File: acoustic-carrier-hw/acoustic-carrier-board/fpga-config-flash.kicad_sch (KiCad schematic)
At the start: 21 parts, among them IC1 ECP5-BGA256, J701 Conn_02x03_Odd_Even, J702 PMOD_JTAG, J703 PMOD_SPI, U701 W25Q128JVS, U702 W25Q128JVS

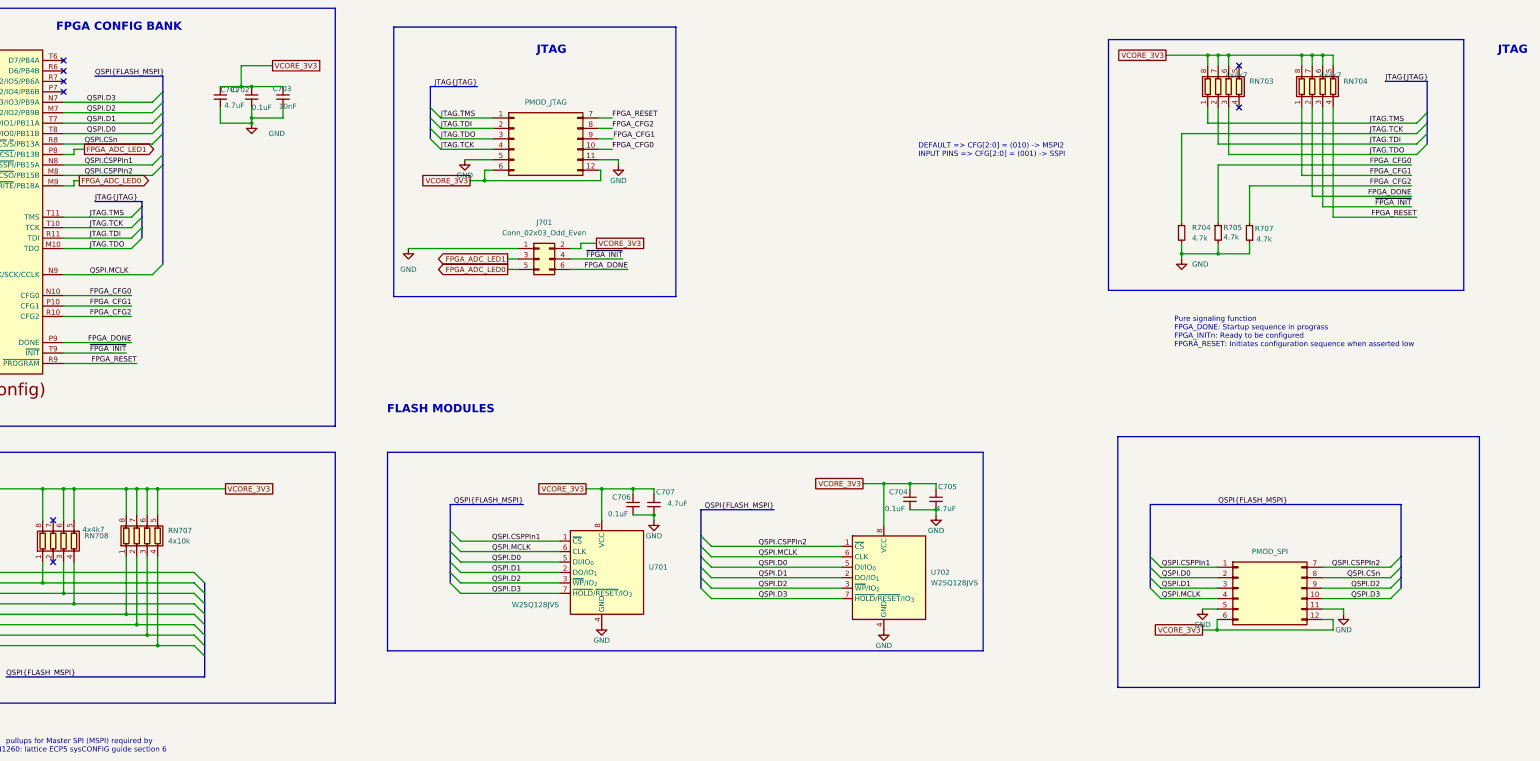
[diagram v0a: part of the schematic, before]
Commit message: [carrier] Added 2 buttons and 2 leds + routing
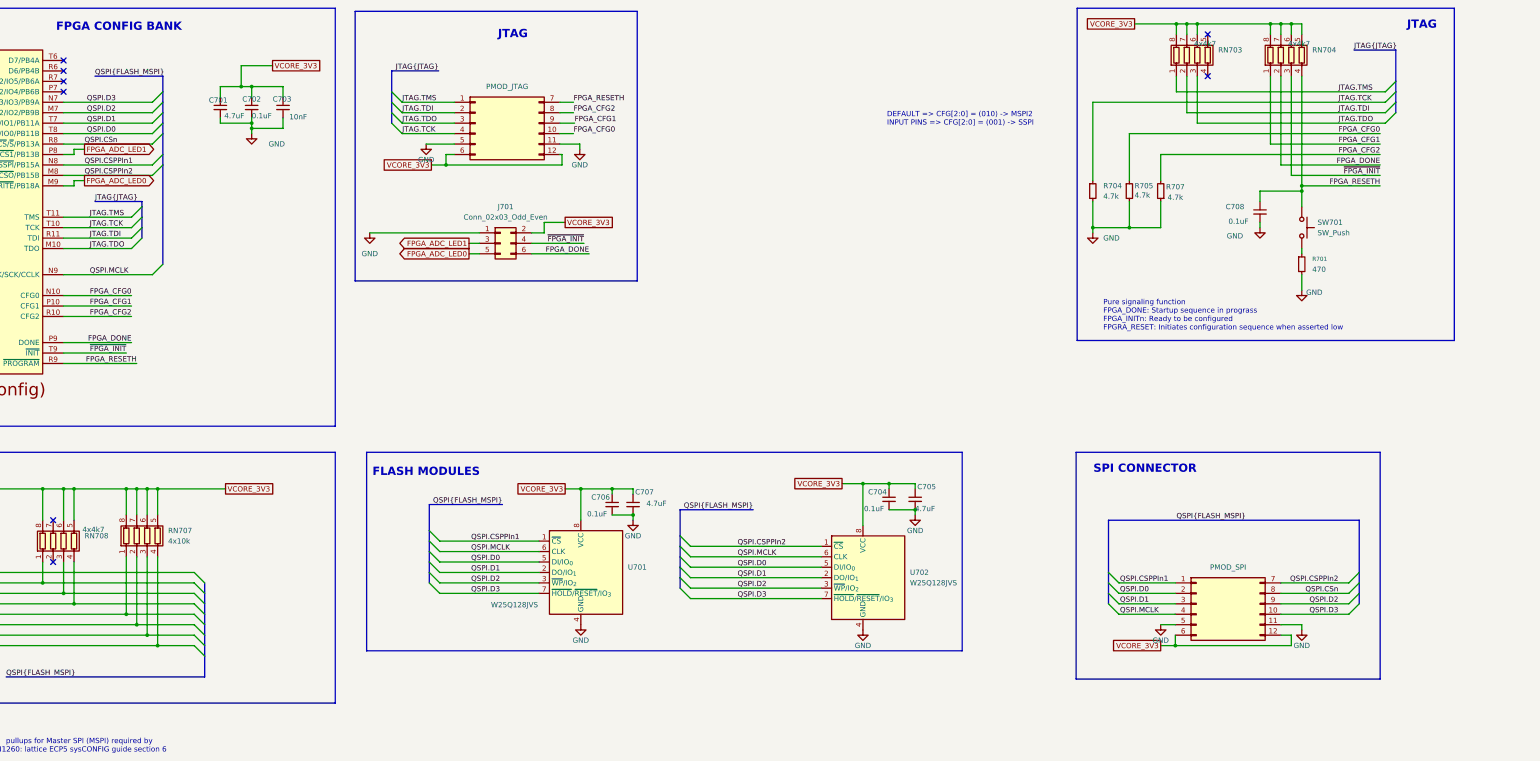
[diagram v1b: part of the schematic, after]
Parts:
- added C708: 0.1uF, Capacitor_SMD:C_0201_0603Metric, symbol Device:C_Small
- added R701: 470, Resistor_SMD:R_0402_1005Metric, symbol Device:R_Small
- added SW701: SW_Push, iw-misc:SW_TS-1088-AR02016, symbol Switch:SW_Push
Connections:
- net GND: now also C708.2, R701.2
- net FPGA_RESET renamed FPGA_RESETH
- net FPGA_RESETH: now also C708.1, SW701.1
- new net: R701.1, SW701.2
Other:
- note added: "SPI CONNECTOR"
- moved on the sheet: C701, C702, C703, C704, C705, C706, C707, J701, R704, R705, R707, RN703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

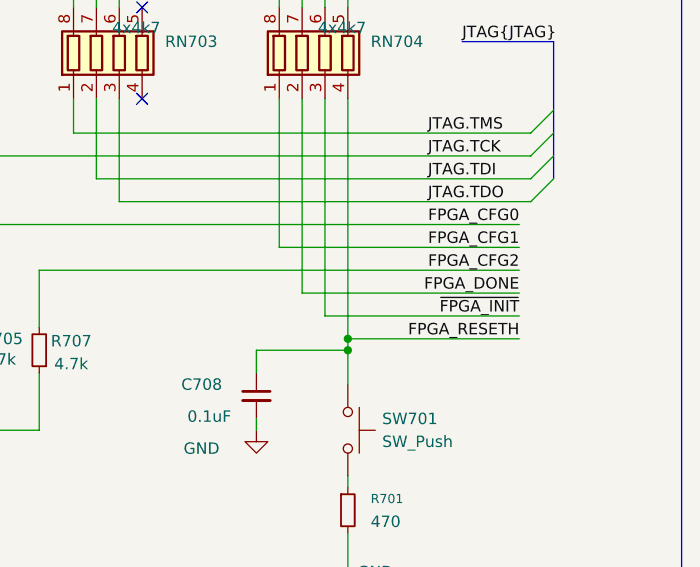
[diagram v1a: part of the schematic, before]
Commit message: [carrier] Added decoupling to LPDDR3 and routed VREF (next) finalize power supply
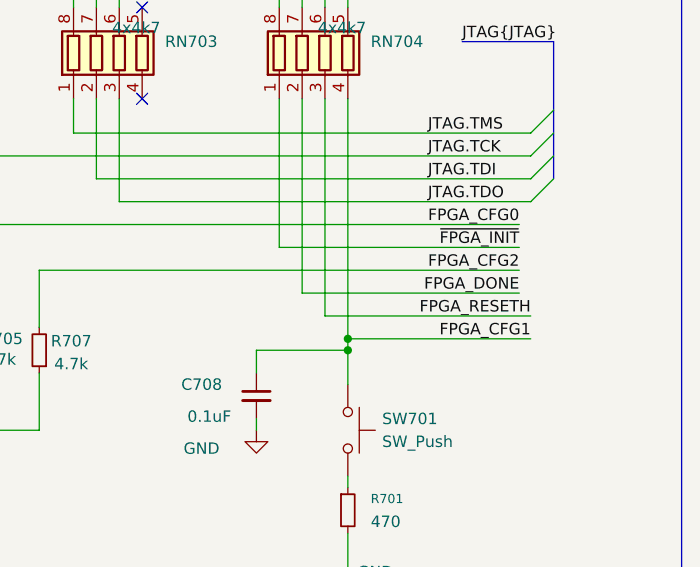
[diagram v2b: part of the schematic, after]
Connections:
- net FPGA_CFG1: now also C708.1, RN704.4 (R4.1), SW701.1; no longer RN704.1 (R1.1)
- net FPGA_RESETH: now also RN704.3 (R3.1); no longer C708.1, RN704.4 (R4.1), SW701.1
- net ~{FPGA_INIT}: now also RN704.1 (R1.1); no longer RN704.3 (R3.1)
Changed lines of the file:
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@@
 	(wire
 		(pts
-			(xy 381 59.69) (xy 361.95 59.69)
+			(xy 361.95 59.69) (xy 382.27 59.69)
 		)
 		(stroke
@@
 	(wire
 		(pts
-			(xy 381 54.61) (xy 356.87 54.61)
+			(xy 356.87 54.61) (xy 381 54.61)
 		)
 		(stroke
@@
 	(wire
 		(pts
-			(xy 381 57.15) (xy 359.41 57.15)
+			(xy 359.41 57.15) (xy 382.27 57.15)
 		)
 		(stroke
@@
 	(wire
 		(pts
-			(xy 381 49.53) (xy 354.33 49.53)
+			(xy 354.33 49.53) (xy 381 49.53)
 		)
 		(stroke
@@
 			(width 0)
 			(type default)
+		)
+	)
+	(label "FPGA_DONE"
+		(at 381 54.61 180)
+		(effects
+			(font
+				(size 1.27 1.27)
+			)
+			(justify right bottom)
 		)
 	)
@@
 		)
 	)
-	(label "FPGA_CFG1"
-		(at 381 49.53 180)
-		(effects
-			(font
-				(size 1.27 1.27)
-			)
-			(justify right bottom)
-		)
-	)
 	(label "JTAG.TMS"
 		(at 143.256 39.37 0)
@@
 		)
 	)
-	(label "FPGA_DONE"
-		(at 381 54.61 180)
-		(effects
-			(font
-				(size 1.27 1.27)
-			)
-			(justify right bottom)
-		)
-	)
 	(label "FPGA_RESETH"
-		(at 381 59.69 180)
+		(at 382.27 57.15 180)
 		(effects
 			(font
@@
 		)
 	)
+	(label "FPGA_CFG1"
+		(at 382.27 59.69 180)
+		(effects
+			(font
+				(size 1.27 1.27)
+			)
+			(justify right bottom)
+		)
+	)
 	(label "QSPI.D0"
 		(at 27.94 163.83 0)
@@
 	)
 	(label "~{FPGA_INIT}"
-		(at 381 57.15 180)
-		(effects
-			(font
-				(size 1.27 1.27)
-			)
-			(justify right bottom)
-		)
-	)
-	(label "~{FPGA_INIT}"
 		(at 76.2 100.33 180)
 		(effects
@@
 		)
 	)
+	(label "~{FPGA_INIT}"
+		(at 381 49.53 180)
+		(effects
+			(font
+				(size 1.27 1.27)
+			)
+			(justify right bottom)
+		)
+	)

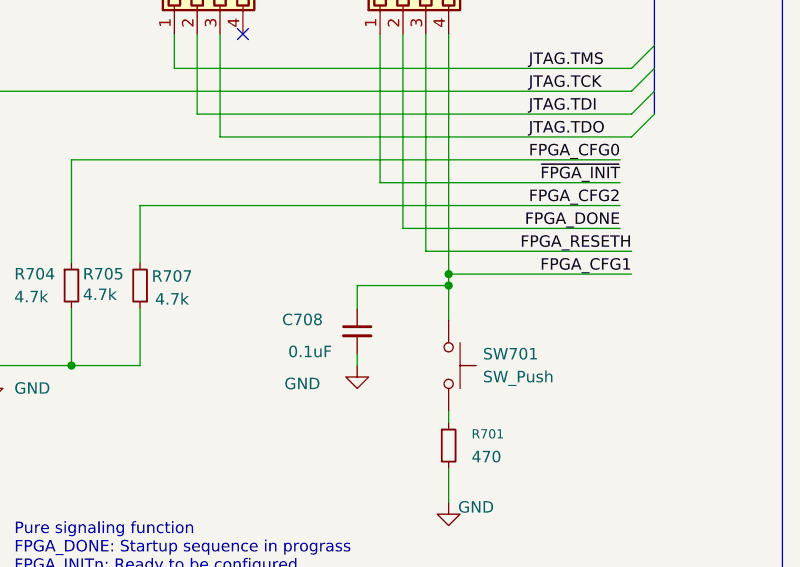
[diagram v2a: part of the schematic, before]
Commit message: [carrier] Corrected most of the DRC errors, a  few tens left + respacing DDR3-traces
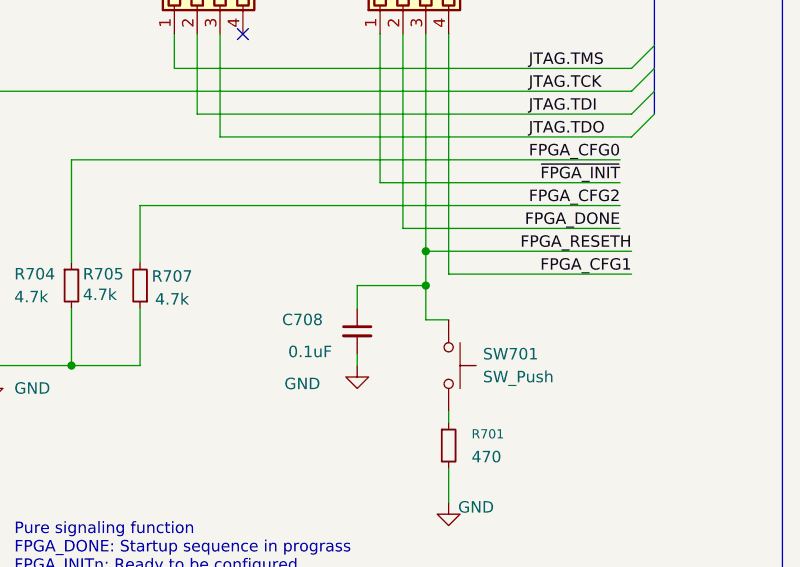
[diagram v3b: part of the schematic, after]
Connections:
- net FPGA_CFG1: no longer C708.1, SW701.1
- net FPGA_RESETH: now also C708.1, SW701.1
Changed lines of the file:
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@@
+	)
+	(junction
+		(at 359.41 57.15)
+		(diameter 0)
+		(color 0 0 0 0)
 	)
 	(junction
@@
 	)
 	(junction
-		(at 361.95 60.96)
-		(diameter 0)
-		(color 0 0 0 0)
-	)
-	(junction
 		(at 336.55 20.32)
 		(diameter 0)
@@
 	)
 	(junction
+		(at 359.41 60.96)
+		(diameter 0)
+		(color 0 0 0 0)
+	)
+	(junction
 		(at 194.31 133.35)
 		(diameter 0)
@@
 	(junction
 		(at 60.96 133.35)
-		(diameter 0)
-		(color 0 0 0 0)
-	)
-	(junction
-		(at 361.95 59.69)
 		(diameter 0)
 		(color 0 0 0 0)
@@
 		)
 	)
+	(wire
+		(pts
+			(xy 359.41 60.96) (xy 359.41 64.77)
+		)
+		(stroke
+			(width 0)
+			(type default)
+		)
+	)
 	(bus
 		(pts
@@
 		)
 	)
-	(wire
-		(pts
-			(xy 361.95 59.69) (xy 361.95 60.96)
-		)
-		(stroke
-			(width 0)
-			(type default)
-		)
-	)
 	(bus
 		(pts
@@
 	(wire
 		(pts
+			(xy 356.87 20.32) (xy 356.87 22.86)
+		)
+		(stroke
+			(width 0)
+			(type default)
+		)
+	)
+	(wire
+		(pts
+			(xy 63.5 50.8) (xy 63.5 52.07)
+		)
+		(stroke
+			(width 0)
+			(type default)
+		)
+	)
+	(bus
+		(pts
+			(xy 210.82 138.43) (xy 210.82 144.78)
+		)
+		(stroke
+			(width 0)
+			(type default)
+		)
+	)
+	(bus
+		(pts
+			(xy 375.92 153.67) (xy 375.92 156.21)
+		)
+		(stroke
+			(width 0)
+			(type default)
+		)
+	)
+	(wire
+		(pts
+			(xy 76.2 133.35) (xy 78.74 133.35)
+		)
+		(stroke
+			(width 0)
+			(type default)
+		)
+	)
+	(wire
+		(pts
+			(xy 331.47 36.83) (xy 382.27 36.83)
+		)
+		(stroke
+			(width 0)
+			(type default)
+		)
+	)
+	(wire
+		(pts
+			(xy 55.88 133.35) (xy 55.88 140.97)
+		)
+		(stroke
+			(width 0)
+			(type default)
+		)
+	)
+	(wire
+		(pts
+			(xy 27.94 161.29) (xy 63.5 161.29)
+		)
+		(stroke
+			(width 0)
+			(type default)
+		)
+	)
+	(wire
+		(pts
+			(xy 83.82 149.86) (xy 83.82 171.45)
+		)
+		(stroke
+			(width 0)
+			(type default)
+		)
+	)
+	(wire
+		(pts
+			(xy 27.94 153.67) (xy 41.91 153.67)
+		)
+		(stroke
+			(width 0)
+			(type default)
+		)
+	)
+	(wire
+		(pts
+			(xy 60.96 102.87) (xy 78.74 102.87)
+		)
+		(stroke
+			(width 0)
+			(type default)
+		)
+	)
+	(wire
+		(pts
+			(xy 336.55 22.86) (xy 336.55 20.32)
+		)
+		(stroke
+			(width 0)
+			(type default)
+		)
+	)
+	(wire
+		(pts
+			(xy 143.256 41.91) (xy 155.956 41.91)
+		)
+		(stroke
+			(width 0)
+			(type default)
+		)
+	)
+	(wire
+		(pts
+			(xy 27.94 166.37) (xy 78.74 166.37)
+		)
+		(stroke
+			(width 0)
+			(type default)
+		)
+	)
+	(bus
+		(pts
+			(xy 68.58 33.02) (xy 85.09 33.02)
+		)
+		(stroke
+			(width 0)
+			(type default)
+		)
+	)
+	(wire
+		(pts
+			(xy 354.33 20.32) (xy 356.87 20.32)
+		)
+		(stroke
+			(width 0)
+			(type default)
+		)
+	)
+	(wire
+		(pts
+			(xy 114.3 45.72) (xy 114.3 43.18)
+		)
+		(stroke
+			(width 0)
+			(type default)
+		)
+	)
+	(wire
+		(pts
+			(xy 60.96 133.35) (xy 60.96 140.97)
+		)
+		(stroke
+			(width 0)
+			(type default)
+		)
+	)
+	(wire
+		(pts
+			(xy 213.36 157.48) (xy 245.11 157.48)
+		)
+		(stroke
+			(width 0)
+			(type default)
+		)
+	)
+	(wire
+		(pts
+			(xy 186.69 133.35) (xy 186.69 140.97)
+		)
+		(stroke
+			(width 0)
+			(type default)
+		)
+	)
+	(wire
+		(pts
 			(xy 361.95 33.02) (xy 361.95 59.69)
 		)
@@
 	(wire
 		(pts
-			(xy 356.87 20.32) (xy 356.87 22.86)
-		)
-		(stroke
-			(width 0)
-			(type default)
-		)
-	)
-	(wire
-		(pts
-			(xy 63.5 50.8) (xy 63.5 52.07)
-		)
-		(stroke
-			(width 0)
-			(type default)
-		)
-	)
-	(bus
-		(pts
-			(xy 210.82 138.43) (xy 210.82 144.78)
-		)
-		(stroke
-			(width 0)
-			(type default)
-		)
-	)
-	(bus
-		(pts
-			(xy 375.92 153.67) (xy 375.92 156.21)
-		)
-		(stroke
-			(width 0)
-			(type default)
-		)
-	)
-	(wire
-		(pts
-			(xy 76.2 133.35) (xy 78.74 133.35)
-		)
-		(stroke
-			(width 0)
-			(type default)
-		)
-	)
-	(wire
-		(pts
-			(xy 331.47 36.83) (xy 382.27 36.83)
-		)
-		(stroke
-			(width 0)
-			(type default)
-		)
-	)
-	(wire
-		(pts
-			(xy 55.88 133.35) (xy 55.88 140.97)
-		)
-		(stroke
-			(width 0)
-			(type default)
-		)
-	)
-	(wire
-		(pts
-			(xy 361.95 60.96) (xy 361.95 64.77)
-		)
-		(stroke
-			(width 0)
-			(type default)
-		)
-	)
-	(wire
-		(pts
-			(xy 27.94 161.29) (xy 63.5 161.29)
-		)
-		(stroke
-			(width 0)
-			(type default)
-		)
-	)
-	(wire
-		(pts
-			(xy 83.82 149.86) (xy 83.82 171.45)
-		)
-		(stroke
-			(width 0)
-			(type default)
-		)
-	)
-	(wire
-		(pts
-			(xy 27.94 153.67) (xy 41.91 153.67)
-		)
-		(stroke
-			(width 0)
-			(type default)
-		)
-	)
-	(wire
-		(pts
-			(xy 60.96 102.87) (xy 78.74 102.87)
-		)
-		(stroke
-			(width 0)
-			(type default)
-		)
-	)
-	(wire
-		(pts
-			(xy 336.55 22.86) (xy 336.55 20.32)
-		)
-		(stroke
-			(width 0)
-			(type default)
-		)
-	)
-	(wire
-		(pts
-			(xy 143.256 41.91) (xy 155.956 41.91)
-		)
-		(stroke
-			(width 0)
-			(type default)
-		)
-	)
-	(wire
-		(pts
-			(xy 27.94 166.37) (xy 78.74 166.37)
-		)
-		(stroke
-			(width 0)
-			(type default)
-		)
-	)
-	(bus
-		(pts
-			(xy 68.58 33.02) (xy 85.09 33.02)
-		)
-		(stroke
-			(width 0)
-			(type default)
-		)
-	)
-	(wire
-		(pts
-			(xy 354.33 20.32) (xy 356.87 20.32)
-		)
-		(stroke
-			(width 0)
-			(type default)
-		)
-	)
-	(wire
-		(pts
-			(xy 114.3 45.72) (xy 114.3 43.18)
-		)
-		(stroke
-			(width 0)
-			(type default)
-		)
-	)
-	(wire
-		(pts
-			(xy 60.96 133.35) (xy 60.96 140.97)
-		)
-		(stroke
-			(width 0)
-			(type default)
-		)
-	)
-	(wire
-		(pts
-			(xy 213.36 157.48) (xy 245.11 157.48)
-		)
-		(stroke
-			(width 0)
-			(type default)
-		)
-	)
-	(wire
-		(pts
-			(xy 186.69 133.35) (xy 186.69 140.97)
-		)
-		(stroke
-			(width 0)
-			(type default)
-		)
-	)
-	(wire
-		(pts
 			(xy 356.87 54.61) (xy 381 54.61)
 		)
@@
 	(wire
 		(pts
-			(xy 351.79 60.96) (xy 361.95 60.96)
+			(xy 351.79 60.96) (xy 359.41 60.96)
 		)
 		(stroke
@@
 	(wire
 		(pts
+			(xy 359.41 57.15) (xy 359.41 60.96)
+		)
+		(stroke
+			(width 0)
+			(type default)
+		)
+	)
+	(wire
+		(pts
 			(xy 106.68 38.1) (xy 106.68 35.56)
 		)
@@
 		)
 		(stroke
+			(width 0)
+			(type default)
+		)
+	)
+	(wire
+		(pts
+			(xy 359.41 64.77) (xy 361.95 64.77)
+		)
+		(stroke
